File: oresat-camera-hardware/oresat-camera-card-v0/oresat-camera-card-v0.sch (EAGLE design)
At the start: 317 parts, among them J1 J-SAMTEC-TFM-120-X1-XXX-D-RA, J2 DM3BT-DSF-PEJS, J4 3-1734592-64-1734592-0, J8 2-1734592-0, Q1 DMP2240UDM, Q3 MIC842, Q4 MIC842, Q5 PMV45EN, Q6 MOSFET-PCH-SOT23-6, Q7 MOSFET-PCH-SOT23-6, Q8 PMV45EN, Q9 MMBT2907, U1 MAX7310ATE, U10 SN74LVC8T245MPWREPPW24-M, U11 RCLAMP0504FB, U12 RCLAMP0504FB, U13 TPS2051CDBVR, U14 TLVH431, U15 SN74LVC1G07DCK, U2 TPS62112, U3 MAX4211CETE, U4 TCAN330, U5 CLVCH16T245MDGGREP, U6 OSD3358-512M-BSM, U7 TCA9509DGKRDGK8-M, U9 TLV70028QDDCRQ1, Y1 24MHz

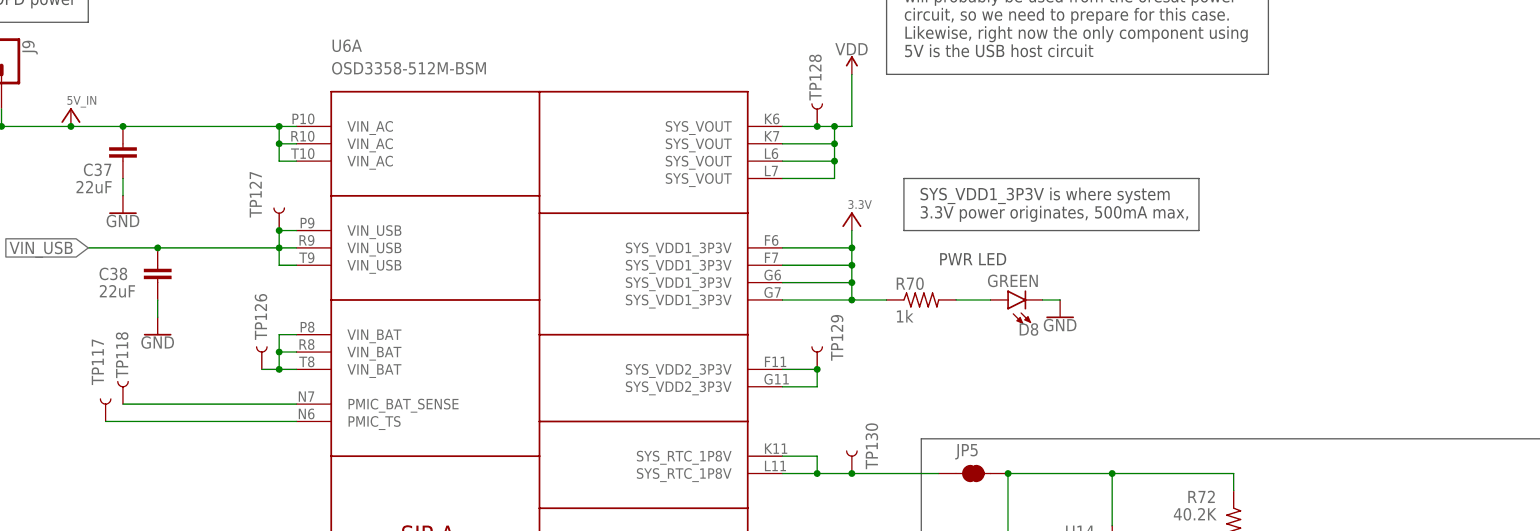
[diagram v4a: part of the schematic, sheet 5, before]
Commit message: added VDD caps
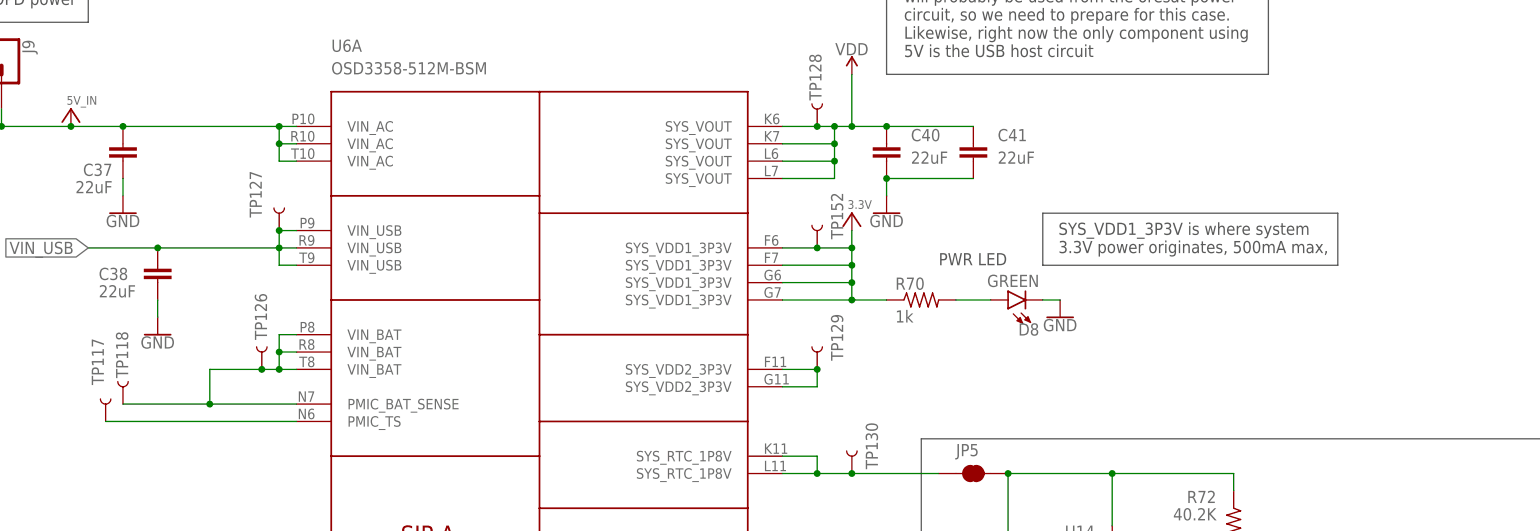
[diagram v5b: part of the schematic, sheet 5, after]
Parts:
- added C40, C41: 22uF, oresat-rcl:C-EUC1210
- added TP152: TEST-POINT3X4, SparkFun-Connectors:TEST-POINT3X4
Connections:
- removed net N$403: TP118.1, U6A.PMIC_BAT_SENSE
- net 3.3V: now also TP152.1
- net GND: now also C40.2, C41.2
- net N$401: now also TP118.1, U6A.PMIC_BAT_SENSE
- net VDD: now also C40.1, C41.1
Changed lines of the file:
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@@
 <part name="TP150" library="Tova" deviceset="TEST-POINT" device=""/>
 <part name="TP151" library="SparkFun-Connectors" deviceset="TEST-POINT" device="3X4"/>
+<part name="TP152" library="SparkFun-Connectors" deviceset="TEST-POINT" device="3X4"/>
+<part name="C40" library="oresat-rcl" deviceset="C-EU" device="C1210" value="22uF"/>
+<part name="GND75" library="SparkFun-PowerSymbols" deviceset="GND" device=""/>
+<part name="C41" library="oresat-rcl" deviceset="C-EU" device="C1210" value="22uF"/>
 </parts>
 <sheets>
@@
 Likewise, right now the only component using
 5V is the USB host circuit</text>
-<text x="-33.274" y="161.798" size="1.778" layer="97">SYS_VDD1_3P3V is where system
+<text x="-12.954" y="156.718" size="1.778" layer="97">SYS_VDD1_3P3V is where system
 3.3V power originates, 500mA max,</text>
 <text x="-30.48" y="154.94" size="1.778" layer="97">PWR LED</text>
@@
 <wire x1="81.28" y1="76.2" x2="-33.02" y2="76.2" width="0.1524" layer="97"/>
 <wire x1="-33.02" y1="76.2" x2="-33.02" y2="129.54" width="0.1524" layer="97"/>
-<wire x1="-35.56" y1="167.64" x2="7.62" y2="167.64" width="0.1524" layer="97"/>
-<wire x1="7.62" y1="167.64" x2="7.62" y2="160.02" width="0.1524" layer="97"/>
-<wire x1="7.62" y1="160.02" x2="-35.56" y2="160.02" width="0.1524" layer="97"/>
-<wire x1="-35.56" y1="160.02" x2="-35.56" y2="167.64" width="0.1524" layer="97"/>
+<wire x1="-15.24" y1="162.56" x2="27.94" y2="162.56" width="0.1524" layer="97"/>
+<wire x1="27.94" y1="162.56" x2="27.94" y2="154.94" width="0.1524" layer="97"/>
+<wire x1="27.94" y1="154.94" x2="-15.24" y2="154.94" width="0.1524" layer="97"/>
+<wire x1="-15.24" y1="154.94" x2="-15.24" y2="162.56" width="0.1524" layer="97"/>
 <wire x1="-38.1" y1="210.82" x2="-38.1" y2="182.88" width="0.1524" layer="97"/>
 <wire x1="-38.1" y1="182.88" x2="17.78" y2="182.88" width="0.1524" layer="97"/>
@@
 <attribute name="NAME" x="-27.94" y="127" size="1.778" layer="95" font="vector"/>
 </instance>
+<instance part="TP152" gate="G$1" x="-48.26" y="157.48" smashed="yes" rot="R90">
+<attribute name="NAME" x="-44.45" y="158.75" size="1.778" layer="95" font="vector" rot="R90"/>
+</instance>
+<instance part="C40" gate="CE" x="-38.1" y="172.72" smashed="yes">
+<attribute name="NAME" x="-34.544" y="173.101" size="1.778" layer="95"/>
+<attribute name="VALUE" x="-34.544" y="169.799" size="1.778" layer="96"/>
+</instance>
+<instance part="GND75" gate="1" x="-38.1" y="162.56" smashed="yes">
+<attribute name="VALUE" x="-38.1" y="162.306" size="1.778" layer="96" align="top-center"/>
+</instance>
+<instance part="C41" gate="CE" x="-25.4" y="172.72" smashed="yes">
+<attribute name="NAME" x="-21.844" y="173.101" size="1.778" layer="95"/>
+<attribute name="VALUE" x="-21.844" y="169.799" size="1.778" layer="96"/>
+</instance>
 </instances>
 <busses>
@@
 <wire x1="-15.24" y1="149.86" x2="-12.7" y2="149.86" width="0.1524" layer="91"/>
 </segment>
+<segment>
+<pinref part="C40" gate="CE" pin="2"/>
+<pinref part="GND75" gate="1" pin="GND"/>
+<wire x1="-38.1" y1="167.64" x2="-38.1" y2="165.1" width="0.1524" layer="91"/>
+<pinref part="C41" gate="CE" pin="2"/>
+<wire x1="-38.1" y1="167.64" x2="-25.4" y2="167.64" width="0.1524" layer="91"/>
+<junction x="-38.1" y="167.64"/>
+</segment>
 </net>
 <net name="VIN_USB" class="0">
@@
 <wire x1="-127" y1="139.7" x2="-129.54" y2="139.7" width="0.1524" layer="91"/>
 <junction x="-127" y="139.7"/>
-</segment>
-</net>
-<net name="N$403" class="0">
-<segment>
+<wire x1="-129.54" y1="139.7" x2="-137.16" y2="139.7" width="0.1524" layer="91"/>
+<junction x="-129.54" y="139.7"/>
 <pinref part="TP118" gate="G$1" pin="1"/>
 <pinref part="U6" gate="A" pin="PMIC_BAT_SENSE"/>
-<wire x1="-149.86" y1="134.62" x2="-124.46" y2="134.62" width="0.1524" layer="91"/>
+<wire x1="-149.86" y1="134.62" x2="-137.16" y2="134.62" width="0.1524" layer="91"/>
+<wire x1="-137.16" y1="134.62" x2="-124.46" y2="134.62" width="0.1524" layer="91"/>
+<wire x1="-137.16" y1="139.7" x2="-137.16" y2="134.62" width="0.1524" layer="91"/>
+<junction x="-137.16" y="134.62"/>
 </segment>
 </net>
@@
 <pinref part="U6" gate="A" pin="SYS_VDD1_3P3V@1"/>
 <pinref part="3V-28" gate="A" pin="3.3V"/>
-<wire x1="-53.34" y1="157.48" x2="-43.18" y2="157.48" width="0.1524" layer="91"/>
+<wire x1="-53.34" y1="157.48" x2="-48.26" y2="157.48" width="0.1524" layer="91"/>
+<wire x1="-48.26" y1="157.48" x2="-43.18" y2="157.48" width="0.1524" layer="91"/>
 <wire x1="-43.18" y1="157.48" x2="-43.18" y2="160.02" width="0.1524" layer="91"/>
 <pinref part="U6" gate="A" pin="SYS_VDD1_3P3V@4"/>
@@
 <wire x1="-43.18" y1="149.86" x2="-38.1" y2="149.86" width="0.1524" layer="91"/>
 <junction x="-43.18" y="149.86"/>
+<pinref part="TP152" gate="G$1" pin="1"/>
+<junction x="-48.26" y="157.48"/>
 </segment>
 </net>
@@
 <pinref part="TP128" gate="G$1" pin="1"/>
 <junction x="-48.26" y="175.26"/>
+<pinref part="C40" gate="CE" pin="1"/>
+<wire x1="-38.1" y1="175.26" x2="-43.18" y2="175.26" width="0.1524" layer="91"/>
+<junction x="-43.18" y="175.26"/>
+<pinref part="C41" gate="CE" pin="1"/>
+<wire x1="-25.4" y1="175.26" x2="-38.1" y2="175.26" width="0.1524" layer="91"/>
+<junction x="-38.1" y="175.26"/>
 </segment>
 </net>

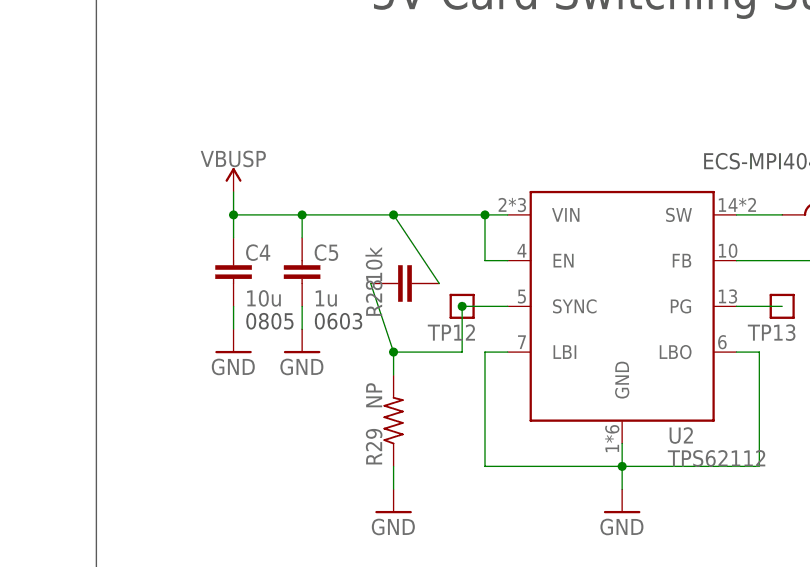
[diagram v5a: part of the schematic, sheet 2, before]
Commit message: added holes for lens mount
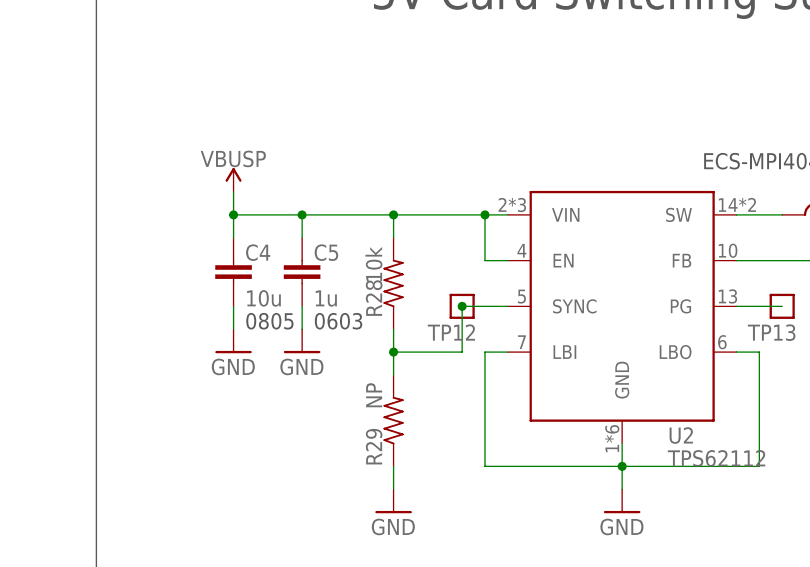
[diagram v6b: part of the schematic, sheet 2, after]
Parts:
- R28: device oresat-rcl:C-EU0603-A -> oresat-rcl:R-US_0603-A
- U8: device U-Generic-eMMC-153pin:EMMC+RESET-BA -> U-Generic-eMMC-153pin:EMMC+RESET+5.1-COMPATIBLE-BA
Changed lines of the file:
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@@
 <part name="C8" library="oresat-rcl" deviceset="C-EU" device="0805-B-NOSILK" value="22u"/>
 <part name="TP15" library="Tova" deviceset="TEST-POINT" device=""/>
-<part name="R28" library="oresat-rcl" deviceset="C-EU" device="0603-A" value="10k">
+<part name="R28" library="oresat-rcl" deviceset="R-US_" device="0603-A" value="10k">
 <attribute name="DIS" value="Digi-Key"/>
 <attribute name="DPN" value="1276-4275-1-ND"/>
@@
 <part name="R58" library="R-Panasonic-EXB_A10PXXXJ" deviceset="EXB-A10P391J" device="C_ARRAY_EXBA-M" value="100K"/>
 <part name="R60" library="R-Panasonic-EXB_A10PXXXJ" deviceset="EXB-A10P391J" device="C_ARRAY_EXBA-M" value="100K"/>
-<part name="U8" library="U-Generic-eMMC-153pin" deviceset="EMMC+RESET" device="-BA"/>
+<part name="U8" library="U-Generic-eMMC-153pin" deviceset="EMMC+RESET+5.1-COMPATIBLE" device="-BA"/>
 <part name="3V-17" library="oresat-supplies" deviceset="3.3V" device=""/>
 <part name="GND44" library="SparkFun-PowerSymbols" deviceset="GND" device=""/>
@@
 <attribute name="NAME" x="284.48" y="87.63" size="1.778" layer="95" font="vector"/>
 </instance>
-<instance part="R28" gate="CE" x="218.44" y="78.74" smashed="yes" rot="R90">
+<instance part="R28" gate="R" x="218.44" y="78.74" smashed="yes" rot="R90">
 <attribute name="DIS" x="218.44" y="78.74" size="1.778" layer="96" rot="R90" display="off"/>
 <attribute name="DPN" x="218.44" y="78.74" size="1.778" layer="96" rot="R90" display="off"/>
@@
 <junction x="226.06" y="76.2"/>
 <pinref part="R29" gate="R" pin="2"/>
-<pinref part="R28" gate="CE" pin="1"/>
+<pinref part="R28" gate="R" pin="1"/>
 <wire x1="218.44" y1="68.58" x2="218.44" y2="71.12" width="0.1524" layer="91"/>
-<wire x1="218.44" y1="71.12" x2="215.9" y2="78.74" width="0.1524" layer="91"/>
+<wire x1="218.44" y1="71.12" x2="218.44" y2="73.66" width="0.1524" layer="91"/>
 <wire x1="226.06" y1="71.12" x2="218.44" y2="71.12" width="0.1524" layer="91"/>
 <junction x="218.44" y="71.12"/>
@@
 <junction x="228.6" y="86.36"/>
 <wire x1="228.6" y1="86.36" x2="218.44" y2="86.36" width="0.1524" layer="91"/>
-<pinref part="R28" gate="CE" pin="2"/>
-<wire x1="223.52" y1="78.74" x2="218.44" y2="86.36" width="0.1524" layer="91"/>
+<pinref part="R28" gate="R" pin="2"/>
+<wire x1="218.44" y1="83.82" x2="218.44" y2="86.36" width="0.1524" layer="91"/>
 <junction x="218.44" y="86.36"/>
 <wire x1="218.44" y1="86.36" x2="208.28" y2="86.36" width="0.1524" layer="91"/>
@@
 </segment>
 </net>
-<net name="N$101" class="0">
+<net name="N$25" class="0">
 <segment>
 <pinref part="Q3" gate="G$1" pin="CIN"/>

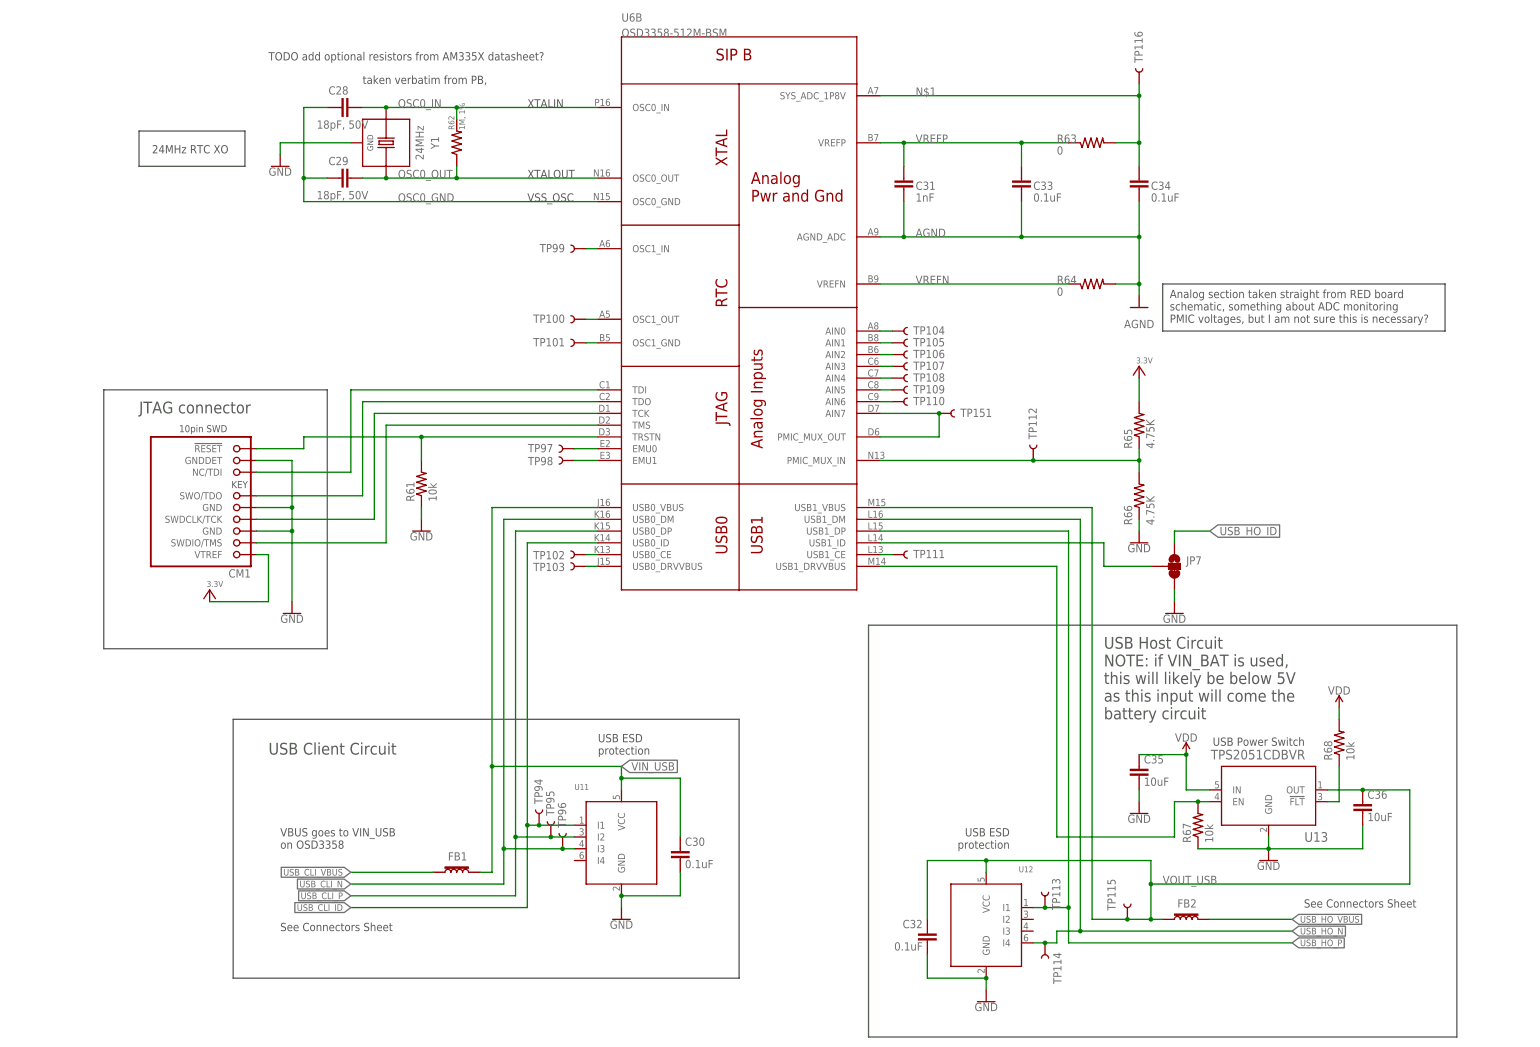
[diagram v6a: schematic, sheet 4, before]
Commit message: update octavo board based on comments from Erik at octavo
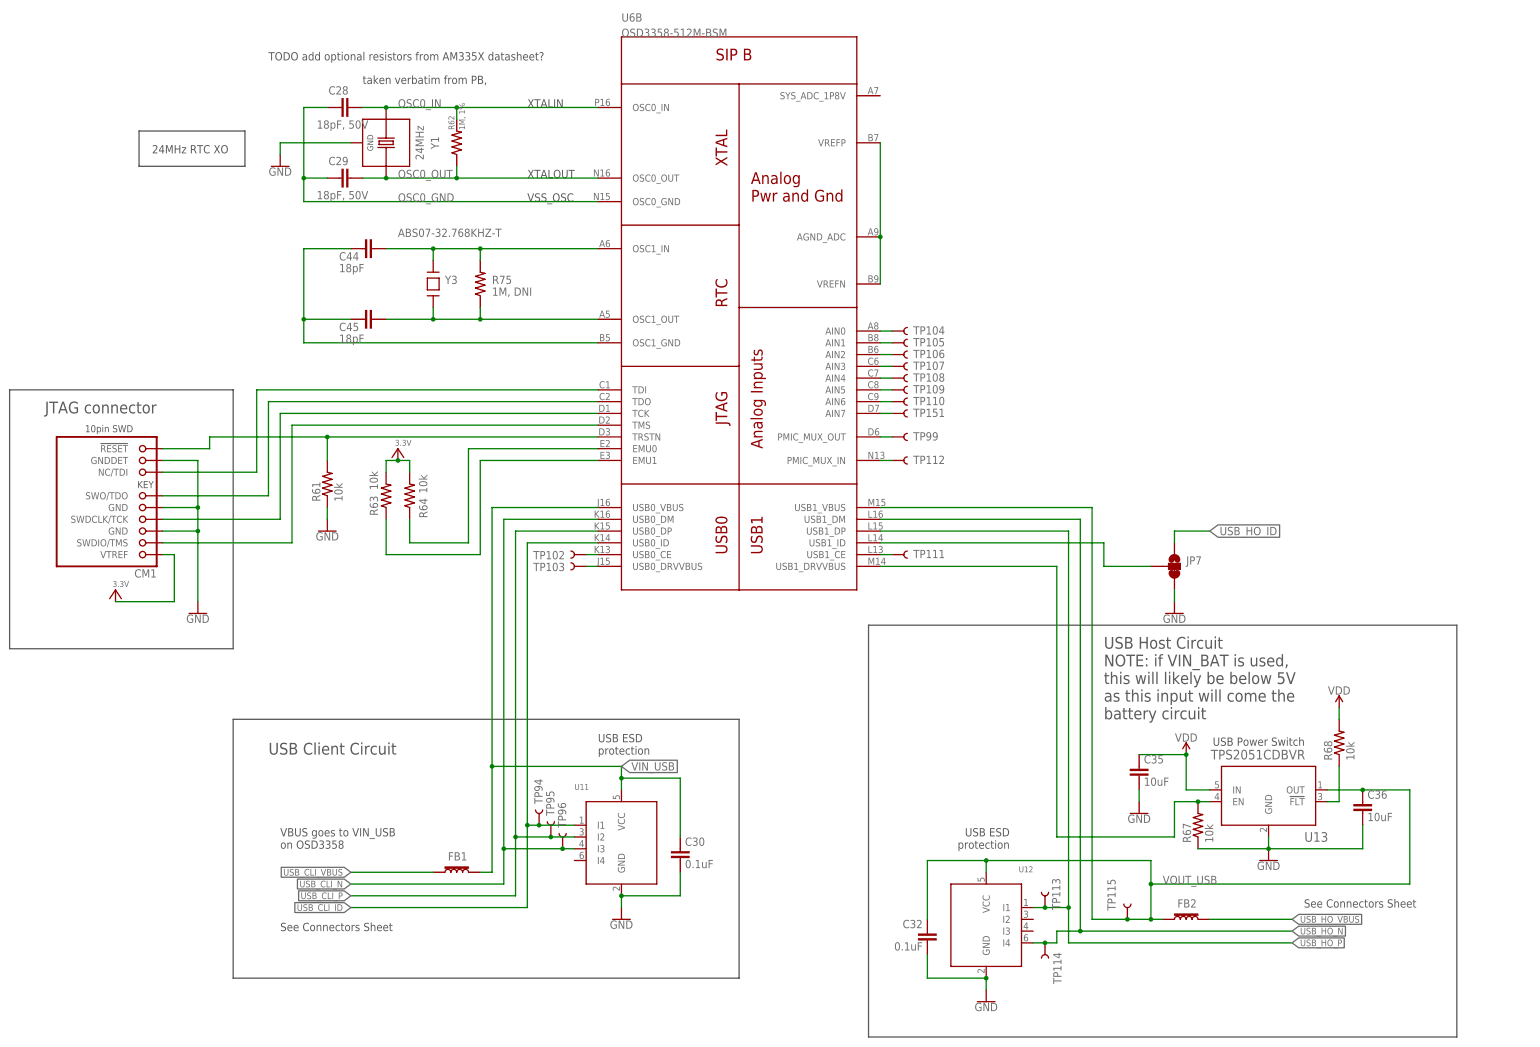
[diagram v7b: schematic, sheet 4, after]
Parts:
- removed C31: 1nF, oresat-rcl:C-EU0603-A
- removed C33, C34: 0.1uF, oresat-rcl:C-EU0603-A
- removed R65, R66: 4.75K, oresat-rcl:R-US_0603-A
- removed TP100, TP101, TP116, TP97, TP98: TEST-POINT3X4, SparkFun-Connectors:TEST-POINT3X4
- added C44, C45: 18pF, oresat-rcl:C-EU0603-A
- added R75: 1M, DNI, oresat-rcl:R-US_0603-A
- added Y3: ABS07-32.768KHZ-T, OSD3358-SM-RED Platform:ABS07-32.768KHZ-T
- R63, R64: value 0 -> 10k
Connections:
- removed net AGND: C31.2, C33.2, C34.2, R64.2, U6B.AGND_ADC
- removed net N$658: TP98.1, U6B.EMU1
- removed net N$659: TP97.1, U6B.EMU0
- removed net N$89: TP99.1, U6B.OSC1_IN
- removed net VDD_RTC: C39.1, TP133.1, U15.VCC
- removed net VREFN: R64.1, U6B.VREFN
- removed net VREFP: C31.1, C33.1, R63.1, U6B.VREFP
- new net N$101: R64.1, U6B.EMU0
- new net OSC1_GND1: C44.2, C45.2, U6B.OSC1_GND
- new net OSC1_IN1: C44.1, R75.2, U6B.OSC1_IN, Y3.P$2
- new net OSC1_OUT1: C45.1, R75.1, U6B.OSC1_OUT, Y3.P$1
- net 3.3V: now also R63.2, R64.2; no longer R65.2
- net GND: no longer R66.1
- net N$1: now also U6B.AGND_ADC, U6B.VREFN, U6B.VREFP; no longer C34.1, R63.2, TP116.1, U6B.SYS_ADC_1P8V
- net N$3: no longer U6B.PMIC_MUX_OUT
- net N$32: now also C39.1, TP133.1, U15.VCC
- net N$90: now also TP99.1, U6B.PMIC_MUX_OUT; no longer TP100.1, U6B.OSC1_OUT
- net N$91: now also R63.1, U6B.EMU1; no longer TP101.1, U6B.OSC1_GND
- net PMIC_MUX_IN: no longer R65.1, R66.2
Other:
- note added: "Power Management Buffer powered from SYS_RTC_1P8V"
- note removed: "Analog section taken straight from RED board schematic, something about ADC monitoring PMIC voltages, but I am not sure this is necessary?"
- moved on the sheet: CM1, R61, R63, R64, TP112, TP151, TP99

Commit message: made a few minor adjustments when I was making the BOMs
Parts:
- removed R12: 10k, oresat-rcl:R-US_0603-A
- C3: value 100n -> 0.1uF
- C4: value 10u -> 10uF
- C44, C45: value 18pF -> 18pF, 50V
- C5, C6: value 1u -> 1uF
- C8: value 22u -> 22uF
- FB1, FB2: MPN (none) -> BLM18KG300JH1D
- J1: value J-SAMTEC-TFM-120-X1-XXX-D-RA -> TFM-120-01-L-D-RA
- R19, R20: value TBD -> 330k
- R21, R22: value TBD -> 1M
- U3: value MAX4211CETE -> MAX4211FETE; MPN MAX4211CETE -> MAX4211FETE
- Y1: MPN (none) -> ECS-240-12-30BQ-AEN-TR
- Y3: MPN (none) -> ABS07-32.768KHZ-T
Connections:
- net GND: no longer R12.1
- net N$480: no longer R12.2
